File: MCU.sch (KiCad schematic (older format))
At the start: 32 parts, among them U10 ESP32-WROOM-32U, U6 STM32F730R8T6, U7 W25Q128JVSIQ, U9 FS35ND01G-S1Y2QWFI000, Y1 Q13FC1350000400, Y2 Crystal_GND24

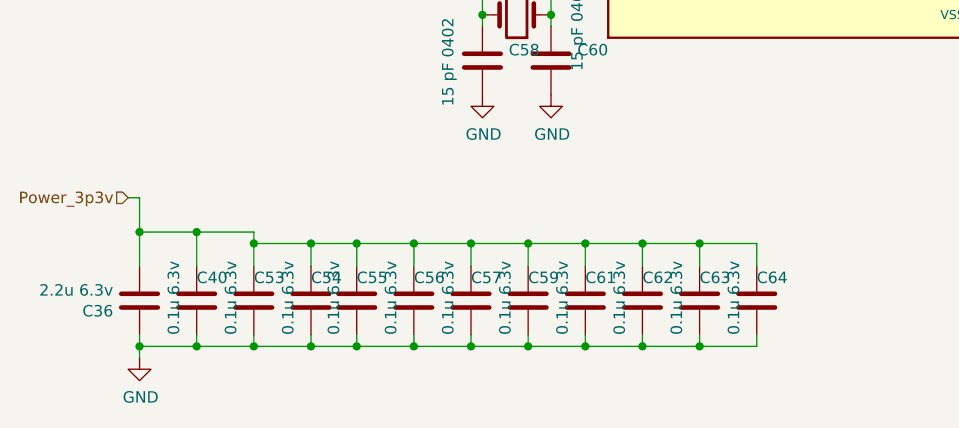
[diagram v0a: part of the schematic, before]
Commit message: Replaced old charger to support JLC assembly. Very close now!
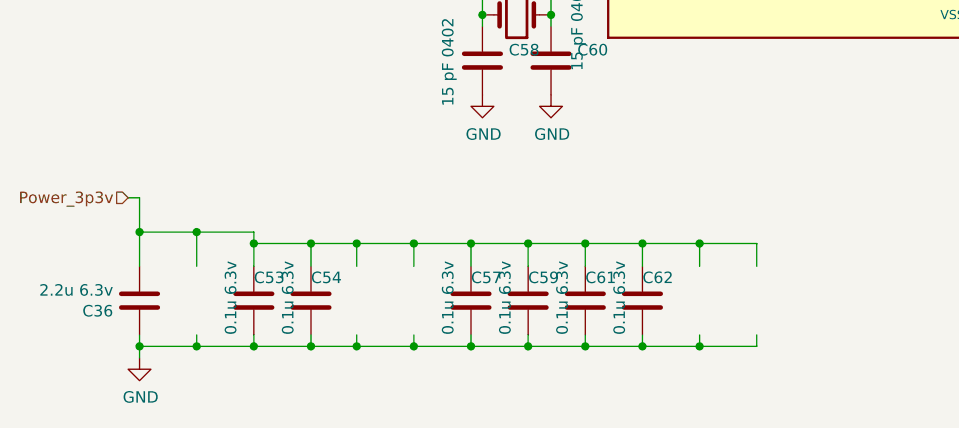
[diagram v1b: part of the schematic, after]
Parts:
- removed C40, C55, C56, C63, C64: 0.1u 6.3v, lc_lib:0402_C, symbol Device:C
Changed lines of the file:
@@
-$Comp
-L Device:C C?
-U 1 1 5FFA2A57
-P 1300 7050
-AR Path="/5FD15753/5FFA2A57" Ref="C?"  Part="1"
-AR Path="/5FF1D194/5FFA2A57" Ref="C40"  Part="1"
-F 0 "C40" H 1300 7150 50  0000 L CNN
-F 1 "0.1u 6.3v" V 1200 6900 50  0000 L CNN
-F 2 "lc_lib:0402_C" H 1338 6900 50  0001 C CNN
-F 3 "~" H 1300 7050 50  0001 C CNN
-	1    1300 7050
-	1    0    0    -1
-$EndComp
 $Comp
 L Device:C C?
@@
 $Comp
 L Device:C C?
-U 1 1 5FFCB597
-P 2000 7050
-AR Path="/5FD15753/5FFCB597" Ref="C?"  Part="1"
-AR Path="/5FF1D194/5FFCB597" Ref="C55"  Part="1"
-F 0 "C55" H 2000 7150 50  0000 L CNN
-F 1 "0.1u 6.3v" V 1900 6900 50  0000 L CNN
-F 2 "lc_lib:0402_C" H 2038 6900 50  0001 C CNN
-F 3 "~" H 2000 7050 50  0001 C CNN
-	1    2000 7050
-	1    0    0    -1
-$EndComp
-$Comp
-L Device:C C?
-U 1 1 5FFCB87A
-P 2250 7050
-AR Path="/5FD15753/5FFCB87A" Ref="C?"  Part="1"
-AR Path="/5FF1D194/5FFCB87A" Ref="C56"  Part="1"
-F 0 "C56" H 2250 7150 50  0000 L CNN
-F 1 "0.1u 6.3v" V 2150 6900 50  0000 L CNN
-F 2 "lc_lib:0402_C" H 2288 6900 50  0001 C CNN
-F 3 "~" H 2250 7050 50  0001 C CNN
-	1    2250 7050
-	1    0    0    -1
-$EndComp
-$Comp
-L Device:C C?
 U 1 1 5FFCBCB0
 P 2500 7050
@@
 	1    0    0    -1
 $EndComp
-$Comp
-L Device:C C?
-U 1 1 5FFCC99C
-P 3500 7050
-AR Path="/5FD15753/5FFCC99C" Ref="C?"  Part="1"
-AR Path="/5FF1D194/5FFCC99C" Ref="C63"  Part="1"
-F 0 "C63" H 3500 7150 50  0000 L CNN
-F 1 "0.1u 6.3v" V 3400 6900 50  0000 L CNN
-F 2 "lc_lib:0402_C" H 3538 6900 50  0001 C CNN
-F 3 "~" H 3500 7050 50  0001 C CNN
-	1    3500 7050
-	1    0    0    -1
-$EndComp
-$Comp
-L Device:C C?
-U 1 1 5FFCCCFF
-P 3750 7050
-AR Path="/5FD15753/5FFCCCFF" Ref="C?"  Part="1"
-AR Path="/5FF1D194/5FFCCCFF" Ref="C64"  Part="1"
-F 0 "C64" H 3750 7150 50  0000 L CNN
-F 1 "0.1u 6.3v" V 3650 6900 50  0000 L CNN
-F 2 "lc_lib:0402_C" H 3788 6900 50  0001 C CNN
-F 3 "~" H 3750 7050 50  0001 C CNN
-	1    3750 7050
-	1    0    0    -1
-$EndComp

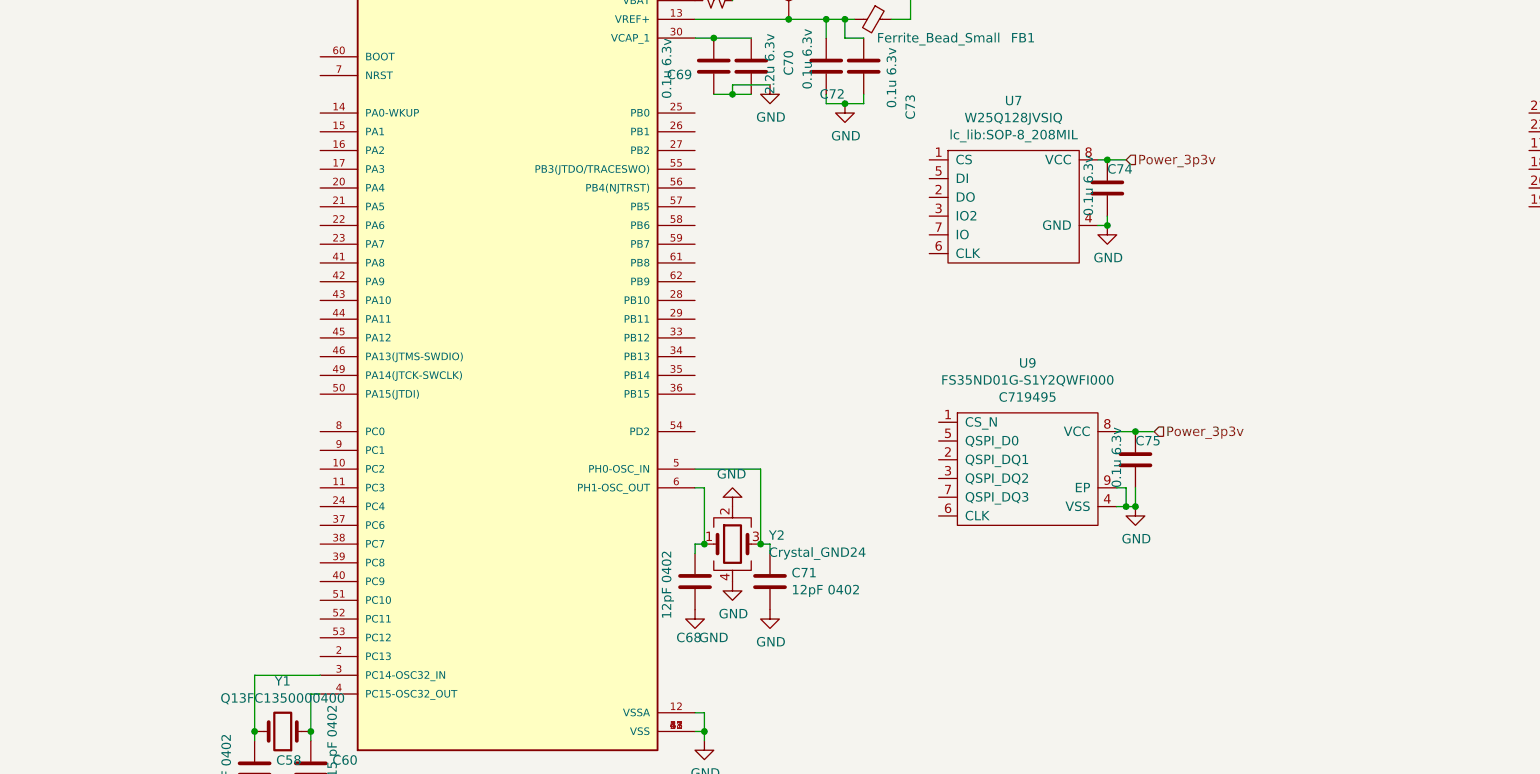
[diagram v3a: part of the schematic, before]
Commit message: Type_A_implemented. Sch "locked". PCB Layout started.
*Changelog:
*Type-a switching regulator (TBD -- need to check inductor,caps, stability. Maybe check both peripherial inductors?)
*Type-A load switch + connector + esd
*started layout..
*found out that my footprint for n fet is wrong. Fixing now, need to replace all of those.
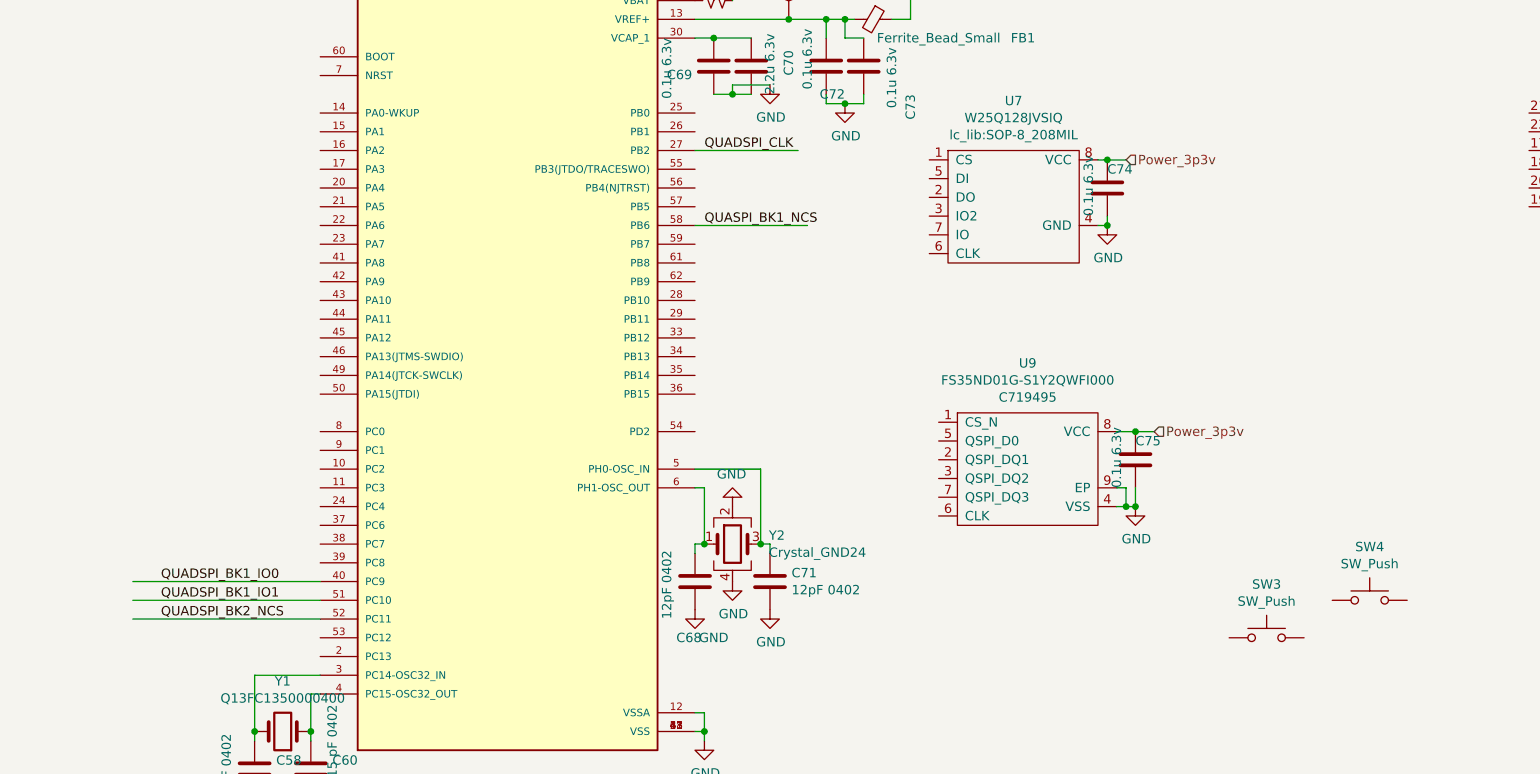
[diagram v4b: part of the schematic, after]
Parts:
- added SW3, SW4: SW_Push, Button_Switch_SMD:SW_Push_1P1T_NO_6x6mm_H9.5mm, symbol Switch:SW_Push
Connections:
- net labels added: QUADSPI_BK1_IO0, QUADSPI_BK1_IO1, QUADSPI_BK2_NCS, QUADSPI_CLK, QUASPI_BK1_NCS
- wire segments 105 -> 110
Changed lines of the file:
@@
 $Descr A4 11693 8268
 encoding utf-8
-Sheet 6 9
+Sheet 6 10
 Title ""
 Date ""
@@
 $EndComp
 Connection ~ 7100 3100
+Wire Wire Line
+	4900 2700 5450 2700
+Text Label 4950 2700 0    50   ~ 0
+QUADSPI_CLK
+Wire Wire Line
+	2900 5100 1900 5100
+Wire Wire Line
+	2900 5200 1900 5200
+Text Label 2050 5100 0    50   ~ 0
+QUADSPI_BK1_IO1
+Text Label 2050 5200 0    50   ~ 0
+QUADSPI_BK2_NCS
+Wire Wire Line
+	4900 3100 5500 3100
+Text Label 4950 3100 0    50   ~ 0
+QUASPI_BK1_NCS
+Text Label 2050 5000 0    50   ~ 0
+QUADSPI_BK1_IO0
+Wire Wire Line
+	2900 5000 1900 5000
+$Comp
+L Switch:SW_Push SW?
+U 1 1 60355B81
+P 7950 5300
+AR Path="/5FD15753/60355B81" Ref="SW?"  Part="1"
+AR Path="/5FF1D194/60355B81" Ref="SW3"  Part="1"
+F 0 "SW3" H 7950 5585 50  0000 C CNN
+F 1 "SW_Push" H 7950 5494 50  0000 C CNN
+F 2 "Button_Switch_SMD:SW_Push_1P1T_NO_6x6mm_H9.5mm" H 7950 5500 50  0001 C CNN
+F 3 "~" H 7950 5500 50  0001 C CNN
+F 4 "TS-1187A-C-G-B" H 7950 5300 50  0001 C CNN "SKU"
+F 5 "C318886" H 7950 5300 50  0001 C CNN "lcsc"
+	1    7950 5300
+	1    0    0    -1
+$EndComp
+$Comp
+L Switch:SW_Push SW?
+U 1 1 60358A5F
+P 8500 5100
+AR Path="/5FD15753/60358A5F" Ref="SW?"  Part="1"
+AR Path="/5FF1D194/60358A5F" Ref="SW4"  Part="1"
+F 0 "SW4" H 8500 5385 50  0000 C CNN
+F 1 "SW_Push" H 8500 5294 50  0000 C CNN
+F 2 "Button_Switch_SMD:SW_Push_1P1T_NO_6x6mm_H9.5mm" H 8500 5300 50  0001 C CNN
+F 3 "~" H 8500 5300 50  0001 C CNN
+F 4 "TS-1187A-C-G-B" H 8500 5100 50  0001 C CNN "SKU"
+F 5 "C318886" H 8500 5100 50  0001 C CNN "lcsc"
+	1    8500 5100
+	1    0    0    -1
+$EndComp
 $EndSCHEMATC

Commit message: Much layout wow.
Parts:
- removed U7: W25Q128JVSIQ, lc_lib:SOP-8_208MIL, symbol SmartBattery:W25Q128JVSIQ
- added D2, D3, D4: LED_BARG, LED_THT:LED_D5.0mm-4_RGB_Wide_Pins, symbol Device:LED_BARG
- added J12: Conn_02x05_Odd_Even, Connector_PinHeader_1.27mm:PinHeader_2x05_P1.27mm_Vertical_SMD, symbol Connector_Generic:Conn_02x05_Odd_Even
- added R111, R112, R113: 100k, lc_lib:0402_R, symbol Device:R_Small_US
- added TP56, TP57, TP58, TP59, TP60: TestPoint, TestPoint:TestPoint_Pad_D2.0mm, symbol Connector:TestPoint
- added U7: LY68L6400SLIT, lc_lib:SOP-8_150MIL, symbol SmartBattery:LY68L6400SLIT
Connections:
- net labels added: ADC1_IN10, ADC1_IN11, ADC1_IN12, ADC1_IN13, ADC1_IN14, ADC_DAC_BUS, BOOT, DAC1, DAC2, ESP32_SCL, ESP32_SDA, ESP32_SERIAL_BL, ESP32_UART_RX, ESP32_UART_TX, ESP32_WAKE, GPIO_BUS, GPIO_ENABLE_ESP32, I2C1_SCL, I2C1_SDA, I2C1_SMBA, I2C2_SCL, I2C2_SDA, NRST, SPI2_MISO, SPI2_MOSI, SPI2_SCK, SWDCLK, SWDIO, SWO, UART5_RX, UART5_TX, USB_FS_DM, USB_FS_DP
- net labels removed: QUADSPI_BK2_NCS
- wire segments 110 -> 194
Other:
- note added: "3p3v for flash"
- note added: "NC to boot BL"
- note added: "RAM 8MB\n"
- note added: "RESET BUTTON\n"
- moved on the sheet: C58, C60, C68, C69, C70, C71, C72, C73, C74, FB1, R33, SW3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

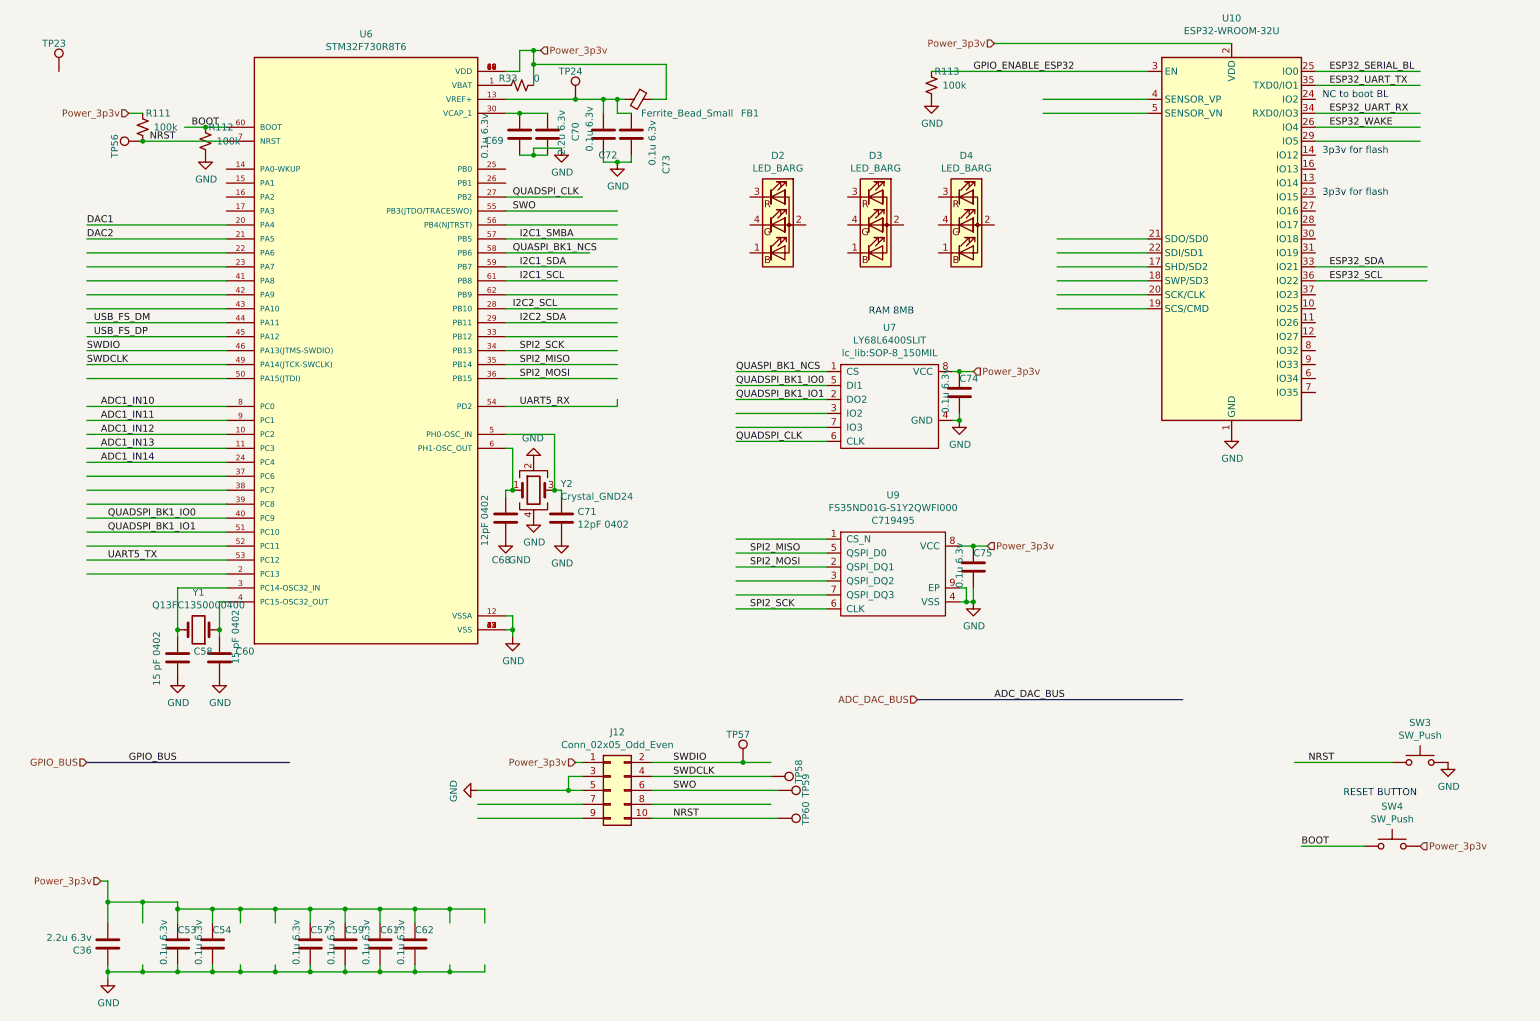
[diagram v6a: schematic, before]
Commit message: Almost connected MCU + ESP32 added leds addedd uart usb cleaned up type-c I/O -- STILL NEED TO level shift I2C
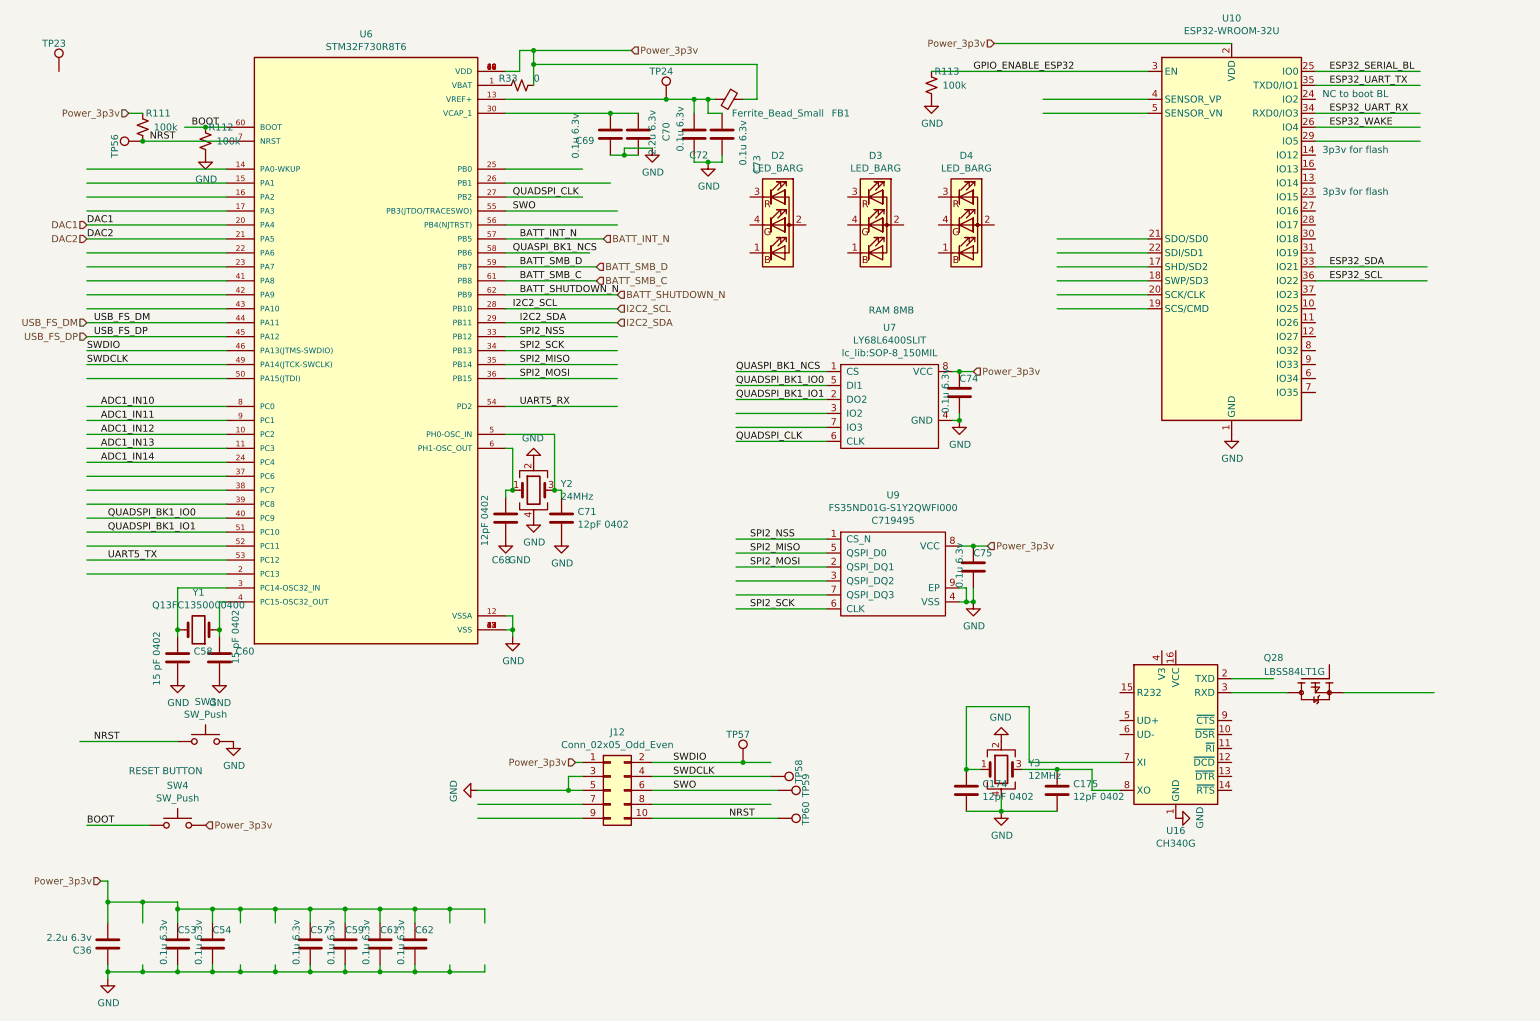
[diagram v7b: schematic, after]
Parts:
- added C174, C175: 12pF 0402, lc_lib:0402_C, symbol Device:C
- added Q28: LBSS84LT1G, lc_lib:SOT-23(SOT-23-3), symbol SmartBattery:VBA2625
- added U16: CH340G, Package_SO:SOIC-16_3.9x9.9mm_P1.27mm, symbol Interface_USB:CH340G
- added Y3: 12MHz, Crystal:Crystal_SMD_3225-4Pin_3.2x2.5mm, symbol Device:Crystal_GND24
- Y2: value Crystal_GND24 -> 24MHz; LCSC C9006 -> C9006
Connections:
- net labels added: BATT_INT_N, BATT_SHUTDOWN_N, BATT_SMB_C, BATT_SMB_D, SPI2_NSS
- net labels removed: ADC_DAC_BUS, GPIO_BUS, I2C1_SCL, I2C1_SDA, I2C1_SMBA
- wire segments 194 -> 214
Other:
- moved on the sheet: C69, C70, C72, C73, FB1, SW3, SW4, TP24
